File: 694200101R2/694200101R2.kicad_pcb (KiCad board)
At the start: 2 copper layers, 438.6 x 125.8 mm, 403 parts, among them J1 USB_C_Receptacle_USB2.0, J2 Conn_01x06_Male, J3 Conn_01x02_Male, SW1 MX_SW, SW10 MX_SW, SW100 MX_SW, SW101 MX_SW, SW102 MX_SW, SW103 MX_SW, SW104 MX_SW, SW105 MX_SW, SW106 MX_SW, SW107 MX_SW, SW11 MX_SW, SW12 MX_SW, SW13 MX_SW, SW14 MX_SW, SW15 MX_SW, SW16 MX_SW, SW17 MX_SW, SW18 MX_SW, SW19 MX_SW, SW2 MX_SW, SW20 MX_SW, SW21 MX_SW, SW22 MX_SW, SW23 MX_SW, SW24 MX_SW, SW25 MX_SW, SW26 MX_SW, SW27 MX_SW, SW28 MX_SW, SW29 MX_SW, SW3 MX_SW, SW30 MX_SW, SW31 MX_SW, SW32 MX_SW, SW33 MX_SW, SW34 MX_SW, SW35 MX_SW, SW36 MX_SW, SW37 MX_SW, SW38 MX_SW, SW39 MX_SW, SW4 MX_SW, SW40 MX_SW, SW41 MX_SW, SW42 MX_SW, SW43 MX_SW, SW44 MX_SW, SW45 MX_SW, SW46 MX_SW, SW47 MX_SW, SW48 MX_SW, SW49 MX_SW, SW5 MX_SW, SW50 MX_SW, SW51 MX_SW, SW52 MX_SW, SW53 MX_SW, SW54 MX_SW, SW55 MX_SW, SW56 MX_SW, SW57 MX_SW, SW58 MX_SW, SW59 MX_SW, SW6 MX_SW, SW60 MX_SW, SW61 MX_SW, SW62 MX_SW, SW63 MX_SW, SW64 MX_SW, SW65 MX_SW, SW66 MX_SW, SW67 MX_SW, SW68 MX_SW, SW69 MX_SW, SW7 MX_SW, SW70 MX_SW, SW71 MX_SW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

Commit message: more squiggles
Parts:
- moved R20 1.28 mm to (349.8, 85.6)
- moved C21 1.27 mm to (343.9, 85.7)
- moved C22 1.27 mm to (343.9, 84.2)
- moved C18 1.27 mm to (341.6, 80.5)
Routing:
- net CS4_B: track 489.1 -> 482.9 mm
- net CS3_B: track 503.9 -> 498.0 mm
- net CS2_B: track 506.6 -> 501.1 mm
- net Net-(R20-Pad1): track 5.51 -> 0.00 mm
- net CS1_B: track 508.1 -> 502.9 mm
- net VCC: track 534.6 -> 531.2 mm
- net SW12_B: track 325.9 -> 323.6 mm
- net SW10_B: track 320.2 -> 318.3 mm
- net SW8_B: track 387.8 -> 386.0 mm
- net CS5_B: track 488.8 -> 487.2 mm
- net CS7_B: track 330.9 -> 329.2 mm
- net SW7_B: track 380.6 -> 379.2 mm
- net SW9_B: track 381.2 -> 379.8 mm
- net CS8_B: track 329.3 -> 328.0 mm
- net SW11_B: track 330.1 -> 328.9 mm
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
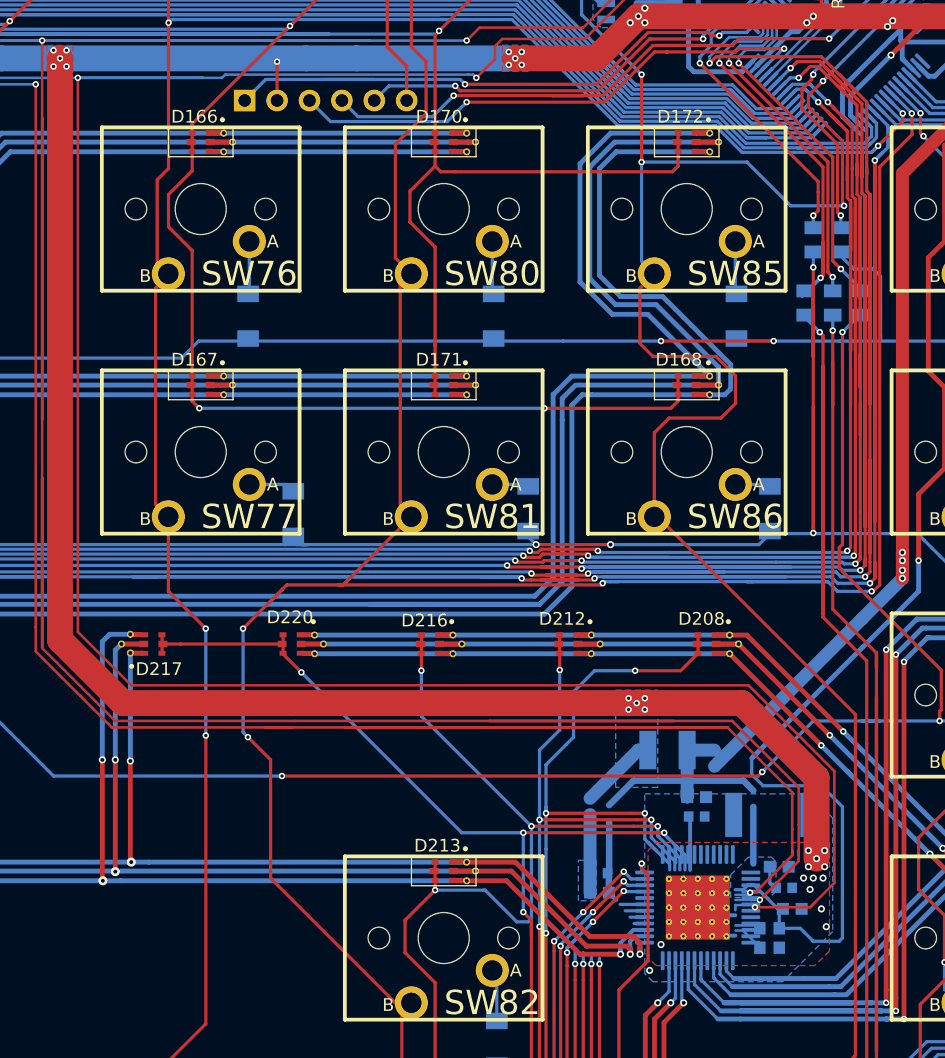
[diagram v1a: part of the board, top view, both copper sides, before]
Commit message: fixing more led drivcer
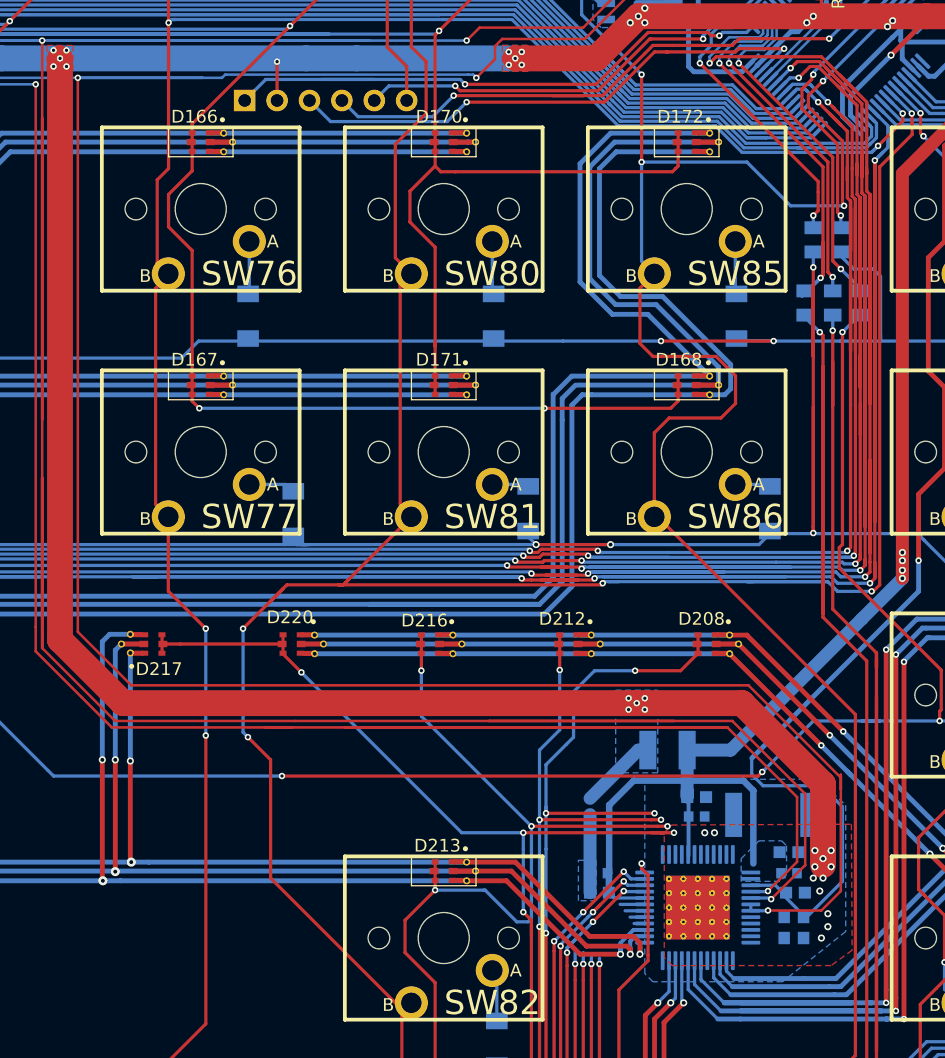
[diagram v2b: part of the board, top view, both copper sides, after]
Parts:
- moved R19 2.10 mm to (351.5, 93.6)
- moved R18 2.05 mm to (351.5, 95.2)
- moved C24 1.37 mm to (351.2, 88.5)
- moved C27 1.30 mm to (351.7, 91.7)
- moved C23 1.20 mm to (351.2, 90.2)
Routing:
- net +3V3: track 819.7 -> 813.2 mm
- net CS9_B: track 317.8 -> 312.4 mm
- net CS10_B: track 337.6 -> 333.7 mm
- net CS11_B: track 316.3 -> 312.9 mm
- net CS12_B: track 254.3 -> 251.0 mm
- net Net-(R18-Pad1): track 2.50 -> 0.00 mm
- net VCC: track 531.2 -> 533.4 mm
- net Net-(R19-Pad2): track 2.01 -> 0.00 mm
- net GND: track 621.2 -> 620.0 mm
- net I2C_SDA: track 1132.7 -> 1131.8 mm
- net SYNC: track 431.2 -> 430.4 mm
- net I2C_SCL: track 457.7 -> 458.4 mm

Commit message: one led drive done, ithink
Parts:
- moved C14 1.69 mm to (33.5, 9.78)
- moved C13 1.67 mm to (32.1, 9.78)
- moved C26 1.25 mm to (30.2, 26.9)
- moved R16 0.92 mm to (28.4, 25.5)
- moved R15 0.89 mm to (26.0, 24.3)
- moved C12 0.54 mm to (32.0, 25.0)
- moved C17 0.51 mm to (41.9, 16.5)
- moved C15 0.51 mm to (37.3, 17.0)
- moved C16 0.51 mm to (39.0, 17.0)
- moved C11 0.40 mm to (33.7, 25.0)
- moved R20 0.13 mm to (349.6, 85.6)
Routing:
- net VCC: track 533.4 -> 519.3 mm
- net I2C_SCL: track 458.4 -> 467.7 mm, vias 5 -> 6
- net CS5_A: track 165.6 -> 159.1 mm
- net SW8_A: track 358.4 -> 363.7 mm
- net Net-(R17-Pad1): track 0.00 -> 5.13 mm
- net SW9_A: track 350.5 -> 355.6 mm
- net SW7_A: track 348.4 -> 353.5 mm
- net CS4_B: track 482.9 -> 487.9 mm
- net I2C_SDA: track 1131.8 -> 1136.7 mm, vias 5 -> 6
- net CS3_B: track 498.0 -> 502.7 mm
- net CS8_A: track 225.9 -> 221.5 mm
- net SYNC: track 430.4 -> 434.8 mm, vias 3 -> 4
- net CS7_A: track 211.4 -> 207.1 mm
- net CS2_B: track 501.1 -> 505.3 mm
- net CS6_A: track 189.5 -> 185.5 mm
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
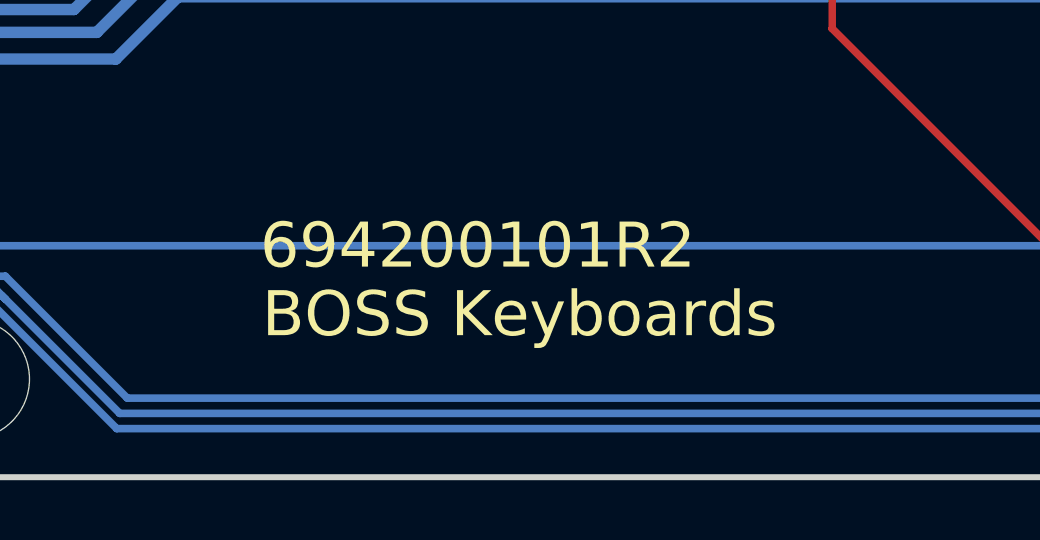
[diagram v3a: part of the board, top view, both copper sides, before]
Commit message: Updated PCB Silkscreen
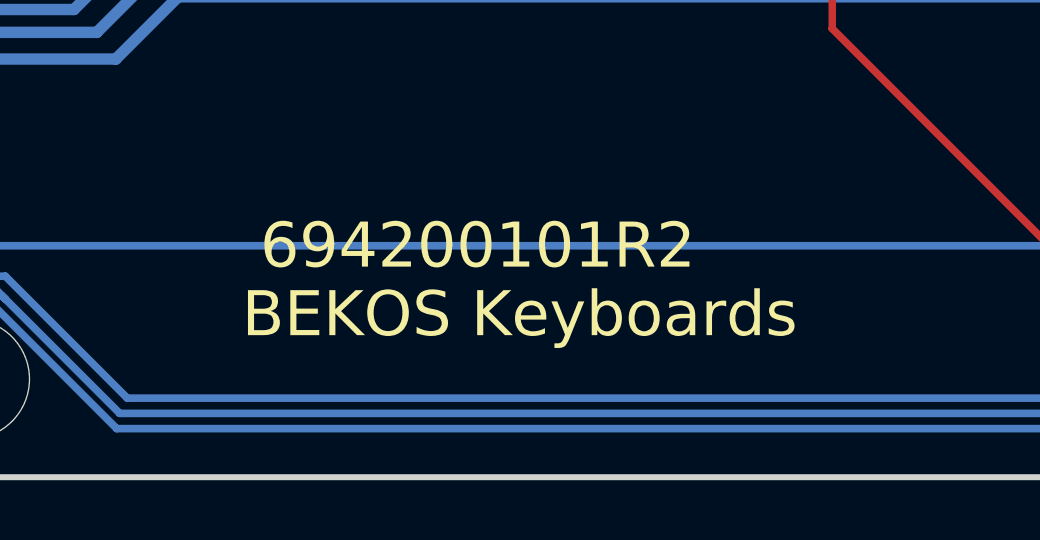
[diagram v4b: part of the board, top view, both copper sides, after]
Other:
- board text added: "BEKOS Keyboards"
- board text removed: "BOSS Keyboards"

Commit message: Fixed Ratsnest errors from prettifying schematic
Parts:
- removed J3: Conn_01x02_Male, Connector_PinHeader_2.54mm:PinHeader_1x02_P2.54mm_Vertical
- removed R11, R13: RNCP0603FTD10K0, Resistor-Libs:RESC1508X50N
- removed R12, R14, R24: MCT06030Z0000ZP500, Resistor-Libs:RESC1508X55N
- added FB2: FBMJ3216HM600-T, Inductor_SMD:L_1206_3216Metric, F.Cu at (411.2, -8.38)
- added SW108: SW_SPST, Button_Switch_SMD:SW_SPST_TL3342, F.Cu at (413.1, -13.6)
- added SW109: SW_SPDT, Button_Switch_SMD:SW_SPDT_CK-JS102011SAQN, F.Cu at (402.8, -12.1)
- C1, C7: footprint capacitor-lib:Samsung-CL10-09_2006-0-IPC_C -> Capacitor_SMD:C_0603_1608Metric
- C10, C5, C9: value CL10B103KB8NNNC -> 10nF; footprint capacitor-lib:Samsung-0603_1608_Metric-0-0-0 -> Capacitor_SMD:C_0603_1608Metric
- C11, C13, C15, C20, C22, C26, C27: value CL10B474KA8NFNC -> 0.47uF; footprint capacitor-lib:CAPC1608X90N -> Capacitor_SMD:C_0603_1608Metric
- C12, C14, C16, C19, C21, C4, C8: value CL10B104KB8NNNL -> 100nF; footprint capacitor-lib:Samsung-CL10-09_2006-0-IPC_C -> Capacitor_SMD:C_0603_1608Metric
- C17, C18: value TAJB226K016RNJ -> 22uF
- C2: value CL10B105KA8NNNC -> 4.7 uF; footprint capacitor-lib:Samsung-CL10-0-0-IPC_C -> Capacitor_SMD:C_0805_2012Metric
- C23: renamed from C24; value CL10B474KA8NFNC -> 100nF; footprint capacitor-lib:CAPC1608X90N -> Capacitor_SMD:C_0603_1608Metric
- C24: renamed from C23; value CL10B104KB8NNNL -> 0.47uF; footprint capacitor-lib:Samsung-CL10-09_2006-0-IPC_C -> Capacitor_SMD:C_0603_1608Metric
- C25: value CL21A475KAQNNNE -> 4.7 uF
- C3, C6: footprint capacitor-lib:AVX-GRM124-0-0-IPC_C -> Capacitor_SMD:C_0603_1608Metric
- ENC1: value PEC11L-4115F-S0020 -> PEC11R-4215F-S0024; footprint SamacSys_Parts:PEC11L4115FS0020 -> digikey-footprints:Rotary_Encoder_Switched_PEC11R
- F1: footprint Fuse:Fuse_1210_3225Metric -> Fuse:Fuse_1210_3225Metric_Castellated
- FB1: value BBUP00160808600Y00 -> FBMJ3216HM600-T; footprint Resistor-Libs:Yageo-RC0603-0-0-IPC_C -> Inductor_SMD:L_1206_3216Metric
- R1, R2: footprint Resistor-Libs:Yageo-RC0603-0-0-IPC_C -> Resistor_SMD:R_0603_1608Metric
- R10, R21, R22, R9: footprint Resistor-Libs:RESC1508X55N -> Resistor_SMD:R_0603_1608Metric
- R15, R16, R18, R19: value RMCF0603FT100K -> 100k; footprint Resistor-Libs:RESC1508X55N -> Resistor_SMD:R_0603_1608Metric
- R17, R20: value RMCF2512FT59K0 -> 59k; footprint Resistor-Libs:RESC6332X70N -> Resistor_SMD:R_2512_6332Metric
- R23: footprint Resistor-Libs:RESC1508X50N -> Resistor_SMD:R_0603_1608Metric
- R3, R4, R5, R6, R7, R8: footprint Resistor-Libs:RESC2012X65N -> Resistor_SMD:R_0805_2012Metric
- U1: value AP2114HA-3.3TRG1 -> AP2114HA-3_3TRG1; footprint DI-LVO:AP2114HA-3.3TRG1 -> digikey-footprints:SOT-223
- U2: footprint cldg:SOT50P160X60-6N -> Package_TO_SOT_SMD:SOT-666
- U4: value M24512-DFMN6TP -> 24LC512; footprint STM:STMicroelectronics-SO8N-SO-A-0-2-MFG -> Package_SO:SO-8_3.9x4.9mm_P1.27mm
- U5, U6: value IS31FL3733B-QFLS4-TR -> IS31FL3733-TQ
- moved ENC1 5.84 mm to (423.9, 9.72)
- turned R18 to 180 degrees
- turned R19 to 0 degrees
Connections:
- net +5V renamed VBUS
- net BOOT0 renamed /BOOT0
- net COL_18 renamed /COL_18
- net CS10_A renamed /LED Drivers/CS10_A
- net CS10_B renamed /LED Drivers/LED Driver B/CS10_B
- net CS11_A renamed /LED Drivers/CS11_A
- net CS11_B renamed /LED Drivers/LED Driver B/CS11_B
- net CS12_A renamed /LED Drivers/CS12_A
- net CS12_B renamed /LED Drivers/LED Driver B/CS12_B
- net CS13_A renamed /LED Drivers/CS13_A
- net CS13_B renamed Net-(U6-Pad30)
- net CS14_A renamed /LED Drivers/CS14_A
- net CS14_B renamed Net-(U6-Pad31)
- net CS15_A renamed /LED Drivers/CS15_A
- net CS15_B renamed Net-(U6-Pad32)
- net CS16_A renamed /LED Drivers/CS16_A
- net CS16_B renamed Net-(U6-Pad33)
- net CS1_A renamed /LED Drivers/CS1_A
- net CS1_B renamed /LED Drivers/LED Driver B/CS1_B
- net CS2_A renamed /LED Drivers/CS2_A
- net CS2_B renamed /LED Drivers/LED Driver B/CS2_B
- net CS3_A renamed /LED Drivers/CS3_A
- net CS3_B renamed /LED Drivers/LED Driver B/CS3_B
- net CS4_A renamed /LED Drivers/CS4_A
- net CS4_B renamed /LED Drivers/LED Driver B/CS4_B
- net CS5_A renamed /LED Drivers/CS5_A
- net CS5_B renamed /LED Drivers/LED Driver B/CS5_B
- net CS6_A renamed /LED Drivers/CS6_A
- net CS6_B renamed /LED Drivers/LED Driver B/CS6_B
- net CS7_A renamed /LED Drivers/CS7_A
- net CS7_B renamed /LED Drivers/LED Driver B/CS7_B
- net CS8_A renamed /LED Drivers/CS8_A
- net CS8_B renamed /LED Drivers/LED Driver B/CS8_B
- net CS9_A renamed /LED Drivers/CS9_A
- net CS9_B renamed /LED Drivers/LED Driver B/CS9_B
- net I2C_SCL renamed /I2C_SCL
- net I2C_SDA renamed /I2C_SDA
- net OSC_IN renamed /OSC_IN
- net OSC_OUT renamed /OSC_OUT
- net ROW_0 renamed /ROW_0
- net ROW_0_MCU renamed /ROW_0_MCU
- net ROW_1 renamed /ROW_1
- net ROW_2 renamed /ROW_2
- net ROW_2_MCU renamed /ROW_2_MCU
- net ROW_3 renamed /ROW_3
- net ROW_3_MCU renamed /ROW_3_MCU
- net ROW_4 renamed /ROW_4
- net ROW_4_MCU renamed /ROW_4_MCU
- net ROW_5 renamed /ROW_5
- net ROW_5_MCU renamed /ROW_5_MCU
- net ROW_6 renamed /ROW_6
- net ROW_6_MCU renamed /ROW_6_MCU
- net SW10_A renamed /LED Drivers/SW10_A
- net SW10_B renamed /LED Drivers/LED Driver B/SW10_B
- net SW11_A renamed /LED Drivers/SW11_A
- net SW11_B renamed /LED Drivers/LED Driver B/SW11_B
- net SW12_A renamed /LED Drivers/SW12_A
- net SW12_B renamed /LED Drivers/LED Driver B/SW12_B
- net SW1_A renamed /LED Drivers/SW1_A
- net SW1_B renamed /LED Drivers/LED Driver B/SW1_B
- net SW2_A renamed /LED Drivers/SW2_A
- net SW2_B renamed /LED Drivers/LED Driver B/SW2_B
- net SW3_A renamed /LED Drivers/SW3_A
- net SW3_B renamed /LED Drivers/LED Driver B/SW3_B
- net SW4_A renamed /LED Drivers/SW4_A
- net SW4_B renamed /LED Drivers/LED Driver B/SW4_B
- net SW5_A renamed /LED Drivers/SW5_A
- net SW5_B renamed /LED Drivers/LED Driver B/SW5_B
- net SW6_A renamed /LED Drivers/SW6_A
- net SW6_B renamed /LED Drivers/LED Driver B/SW6_B
- net SW7_A renamed /LED Drivers/SW7_A
- net SW7_B renamed /LED Drivers/LED Driver B/SW7_B
- net SW8_A renamed /LED Drivers/SW8_A
- net SW8_B renamed /LED Drivers/LED Driver B/SW8_B
- net SW9_A renamed /LED Drivers/SW9_A
- net SW9_B renamed /LED Drivers/LED Driver B/SW9_B
- net SYNC renamed /LED Drivers/SYNC_OUT
- CR1 pad 1: Net-(CR1-Pad1) -> VCC
- F1 pad 1: Net-(CR1-Pad1) -> VCC
- F1 pad 2: VCC -> Net-(F1-Pad2)
- FB1 pad 1: Net-(CR1-Pad1) -> Net-(F1-Pad2)
- R15 pad 1: Net-(R15-Pad1) -> GND
- R15 pad 2: GND -> Net-(R15-Pad2)
- R16 pad 1: +3V3 -> Net-(R16-Pad1)
- R16 pad 2: Net-(R16-Pad2) -> +3V3
- R18 pad 1: Net-(R18-Pad1) -> GND
- R18 pad 2: GND -> Net-(R18-Pad2)
- R19 pad 1: +3V3 -> Net-(R19-Pad1)
- R19 pad 2: Net-(R19-Pad2) -> +3V3
- U5 pad 46: Net-(R16-Pad2) -> Net-(R16-Pad1)
- U5 pad 47: Net-(R15-Pad1) -> Net-(R15-Pad2)
- U6 pad 46: Net-(R19-Pad2) -> Net-(R19-Pad1)
- U6 pad 47: Net-(R18-Pad1) -> Net-(R18-Pad2)
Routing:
- net +3V3: track 812.5 -> 756.1 mm, vias 16 -> 14
- net Net-(CR1-Pad1): track 6.70 -> 0.00 mm
- net VCC: track 519.3 -> 526.0 mm
- net Net-(ENC1-PadA1): track 5.87 -> 0.00 mm
- net Net-(ENC1-PadB1): track 5.72 -> 0.00 mm
- net ENCODER_B: track 81.5 -> 86.6 mm
- net ENCODER_A: track 77.0 -> 82.0 mm
- net Net-(R19-Pad2): track 3.03 -> 0.00 mm
- net Net-(R19-Pad1): track 0.00 -> 3.03 mm
- net Net-(R18-Pad2): track 0.00 -> 2.67 mm
- net Net-(R18-Pad1): track 2.67 -> 0.00 mm
- net GND: track 618.1 -> 619.4 mm, vias 55 -> 56
- net CS8_A: vias 0 -> 1
- net CS7_A: vias 0 -> 1
- net CS6_A: vias 0 -> 1
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
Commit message: Updated Footprints to have CAD Models
Need footprints on board to allow for case modifications
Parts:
- added G***: LOGO, BekosLogo:BekosLogo, F.Cu at (298.5, 95.8)
- C17, C18: footprint capacitor-lib:CAPPC3528X210N -> Capacitor_Tantalum_SMD:CP_EIA-3528-21_Kemet-B
- ENC1: footprint digikey-footprints:Rotary_Encoder_Switched_PEC11R -> cldg:Rotary_Encoder_Switched_PEC11R
- J1: footprint Connector_USB:USB_C_Receptacle_GCT_USB4085 -> cldg:USB_C_Receptacle_GCT_USB4085
- SW109: footprint Button_Switch_SMD:SW_SPDT_CK-JS102011SAQN -> cldg:SW_SPDT_CK-JS102011SAQN
- U1: footprint digikey-footprints:SOT-223 -> Package_TO_SOT_SMD:SOT-223
- U4: footprint Package_SO:SO-8_3.9x4.9mm_P1.27mm -> Package_SO:SOIC-8_3.9x4.9mm_P1.27mm
- turned U1 to 180 degrees
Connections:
- net COL_0 renamed /COL_0
- net COL_1 renamed /COL_1
- net COL_10 renamed /COL_10
- net COL_11 renamed /COL_11
- net COL_12 renamed /COL_12
- net COL_13 renamed /COL_13
- net COL_14 renamed /COL_14
- net COL_15 renamed /COL_15
- net COL_16 renamed /COL_16
- net COL_17 renamed /COL_17
- net COL_19 renamed /COL_19
- net COL_2 renamed /COL_2
- net COL_20 renamed /COL_20
- net COL_21 renamed /COL_21
- net COL_22 renamed /COL_22
- net COL_3 renamed /COL_3
- net COL_4 renamed /COL_4
- net COL_5 renamed /COL_5
- net COL_6 renamed /COL_6
- net COL_7 renamed /COL_7
- net COL_8 renamed /COL_8
- net COL_9 renamed /COL_9
- net ENCODER_A renamed /ENCODER_A
- net ENCODER_B renamed /ENCODER_B
- net Net-(J1-PadA6) renamed /D+
- net Net-(J1-PadA7) renamed /D-
- net RST renamed /RST
- net SWCLK renamed /SWCLK
- net SWDIO renamed /SWDIO
- net SWO renamed /SWO
- net USB_D+ renamed /USB_D+
- net USB_D- renamed /USB_D-
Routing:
- net GND: vias 56 -> 58
